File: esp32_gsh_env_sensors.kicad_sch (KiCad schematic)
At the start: 58 parts, among them J1 USB_C_Receptacle_USB2.0, J2 C50950, J4 C2718488, Q1 SS8050, Q2 SS8050, SW1 EN, SW2 BOOT, SW3 CALIBRATE, U1 MP2359, U2 BME280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

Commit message: Fix MH-Z19B wiring
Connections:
- net IO17/RXD: now also J2.4 (Pin_4); no longer J2.2 (Pin_2)
- net at SW3.2: now also J2.1 (Pin_1); no longer J2.5 (Pin_5)
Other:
- moved on the sheet: SW3
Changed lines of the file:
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@@
   (no_connect (at 191.135 82.55))
   (no_connect (at 191.135 54.61))
-  (no_connect (at 199.39 151.13))
-  (no_connect (at 199.39 143.51))
   (no_connect (at 260.985 66.04))
   (no_connect (at 260.985 60.96))
@@
   (no_connect (at 191.135 90.17))
   (no_connect (at 260.985 53.34))
+  (no_connect (at 199.39 146.05))
+  (no_connect (at 199.39 153.67))
   (no_connect (at 260.985 50.8))
   (no_connect (at 260.985 40.64))
@@
     (stroke (width 0) (type default) (color 0 0 0 0))
   )
-  (wire (pts (xy 179.07 153.67) (xy 179.07 157.48))
+  (wire (pts (xy 179.07 143.51) (xy 179.07 147.32))
     (stroke (width 0) (type default) (color 0 0 0 0))
   )
@@
     (stroke (width 0) (type default) (color 0 0 0 0))
   )
-  (wire (pts (xy 189.23 153.67) (xy 199.39 153.67))
+  (wire (pts (xy 189.23 143.51) (xy 199.39 143.51))
     (stroke (width 0) (type default) (color 0 0 0 0))
   )
@@
     (stroke (width 0) (type default) (color 0 0 0 0))
   )
-  (wire (pts (xy 189.865 146.05) (xy 199.39 146.05))
+  (wire (pts (xy 189.865 151.13) (xy 199.39 151.13))
     (stroke (width 0) (type default) (color 0 0 0 0))
   )
@@
     (effects (font (size 1.27 1.27)) (justify right bottom))
   )
-  (label "IO17{slash}RXD" (at 189.865 146.05 0)
+  (label "IO17{slash}RXD" (at 189.865 151.13 0)
     (effects (font (size 1.27 1.27)) (justify left bottom))
   )
@@
     (pin "2")
   )
-  (symbol (lib_id "Switch:SW_Push") (at 184.15 153.67 0) (unit 1)
+  (symbol (lib_id "Switch:SW_Push") (at 184.15 143.51 0) (unit 1)
     (in_bom yes) (on_board yes) (fields_autoplaced)
-    (property "Reference" "SW3" (id 0) (at 184.15 146.05 0))
-    (property "Value" "CALIBRATE" (id 1) (at 184.15 148.59 0))
-    (property "Footprint" "Button_Switch_SMD:SW_Push_SPST_NO_Alps_SKRK" (id 2) (at 184.15 148.59 0)
-      (effects (font (size 1.27 1.27)) hide)
-    )
-    (property "Datasheet" "~" (id 3) (at 184.15 148.59 0)
-      (effects (font (size 1.27 1.27)) hide)
-    )
-    (property "LCSC" "C115357" (id 4) (at 184.15 153.67 0)
+    (property "Reference" "SW3" (id 0) (at 184.15 135.89 0))
+    (property "Value" "CALIBRATE" (id 1) (at 184.15 138.43 0))
+    (property "Footprint" "Button_Switch_SMD:SW_Push_SPST_NO_Alps_SKRK" (id 2) (at 184.15 138.43 0)
+      (effects (font (size 1.27 1.27)) hide)
+    )
+    (property "Datasheet" "~" (id 3) (at 184.15 138.43 0)
+      (effects (font (size 1.27 1.27)) hide)
+    )
+    (property "LCSC" "C115357" (id 4) (at 184.15 143.51 0)
       (effects (font (size 1.27 1.27)) hide)
     )
@@
     (pin "2")
   )
-  (symbol (lib_id "power:GND") (at 179.07 157.48 0) (unit 1)
+  (symbol (lib_id "power:GND") (at 179.07 147.32 0) (unit 1)
     (in_bom yes) (on_board yes) (fields_autoplaced)
-    (property "Reference" "#PWR029" (id 0) (at 179.07 163.83 0)
-      (effects (font (size 1.27 1.27)) hide)
-    )
-    (property "Value" "GND" (id 1) (at 179.07 162.56 0))
-    (property "Footprint" "" (id 2) (at 179.07 157.48 0)
-      (effects (font (size 1.27 1.27)) hide)
-    )
-    (property "Datasheet" "" (id 3) (at 179.07 157.48 0)
-      (effects (font (size 1.27 1.27)) hide)
-    )
+    (property "Reference" "#PWR029" (id 0) (at 179.07 153.67 0)
+      (effects (font (size 1.27 1.27)) hide)
+    )
+    (property "Value" "GND" (id 1) (at 179.07 152.4 0))
+    (property "Footprint" "" (id 2) (at 179.07 147.32 0)
+      (effects (font (size 1.27 1.27)) hide)
+    )
+    (property "Datasheet" "" (id 3) (at 179.07 147.32 0)
+      (effects (font (size 1.27 1.27)) hide)
+    )

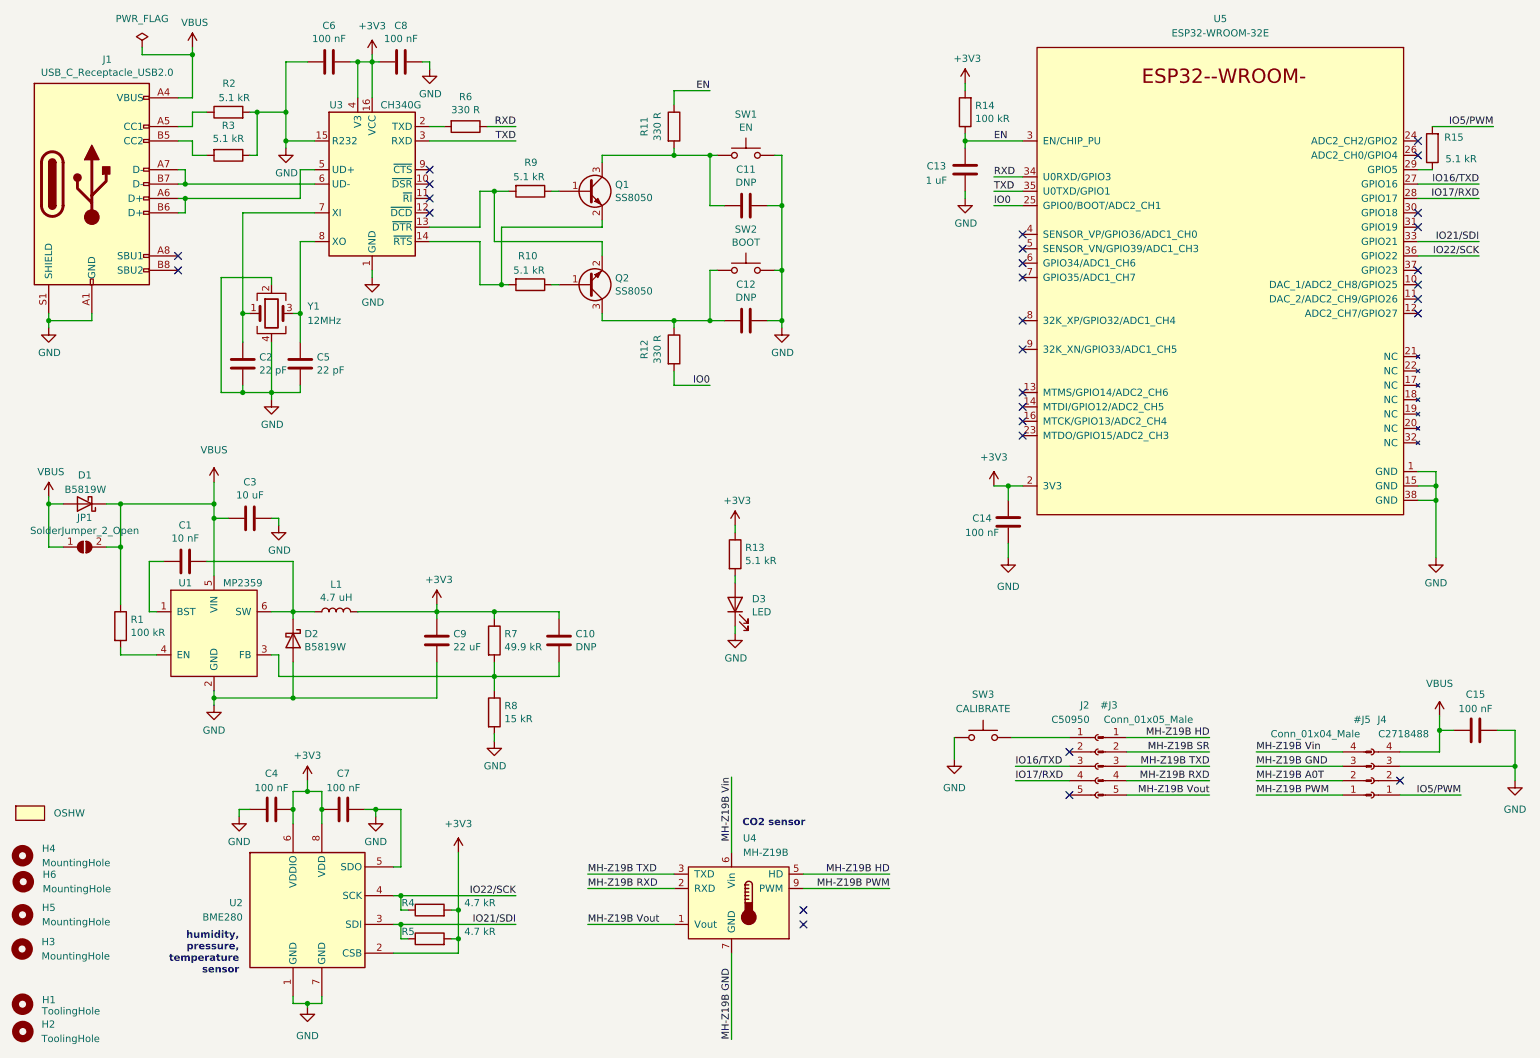
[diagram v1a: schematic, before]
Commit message: Change MH-Z19B power input to VCC
This is required to protect attaced USB equipment
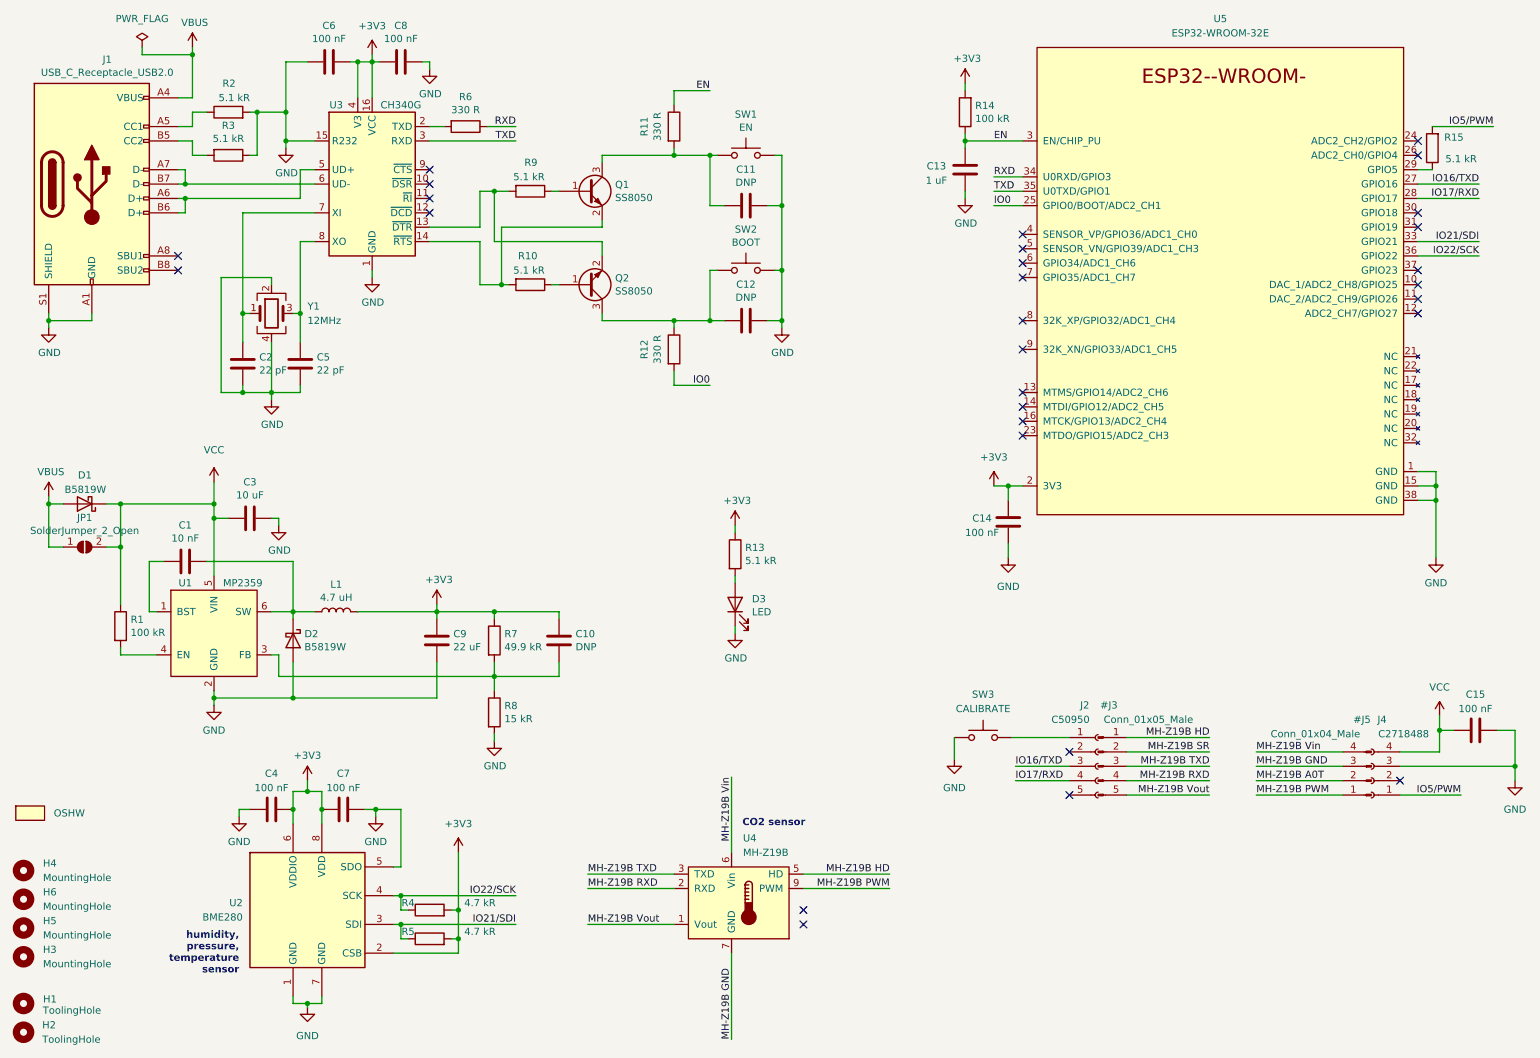
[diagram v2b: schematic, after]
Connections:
- net VBUS: no longer C15.1, C3.2, D1.1 (K), J4.4 (Pin_4), JP1.2 (B), R1.1, U1.5 (VIN)
- new net VCC: C15.1, C3.2, D1.1 (K), J4.4 (Pin_4), JP1.2 (B), R1.1, U1.5 (VIN)
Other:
- moved on the sheet: H3, H4, H5, H6
